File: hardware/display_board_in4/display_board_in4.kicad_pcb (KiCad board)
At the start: 4 copper layers, 250 x 50 mm, 169 parts, among them J1 CTRL, J2 HV_INPUT, J3 LED_CTRL, Q1 MMBTA42, Q10 MMBTA42, Q11 MMBTA42, Q12 MMBTA42, Q13 MMBTA42, Q14 MMBTA42, Q15 MMBTA42, Q16 MMBTA42, Q17 MMBTA42, Q18 MMBTA42, Q19 MMBTA42, Q2 MMBTA42, Q20 MMBTA42, Q21 MMBTA42, Q22 MMBTA42, Q23 MMBTA42, Q24 MMBTA42, Q25 MMBTA42, Q26 MMBTA42, Q27 MMBTA42, Q28 MMBTA42, Q29 MMBTA42, Q3 MMBTA42, Q30 MMBTA42, Q31 MMBTA42, Q32 MMBTA42, Q33 MMBTA42, Q34 MMBTA42, Q35 MMBTA42, Q36 MMBTA42, Q37 MMBTA42, Q38 MMBTA42, Q39 MMBTA42, Q4 MMBTA42, Q40 MMBTA42, Q41 MMBTA42, Q42 MMBTA42, Q43 MMBTA42, Q44 MMBTA42, Q45 MMBTA42, Q46 MMBTA42, Q47 MMBTA42, Q48 MMBTA42, Q49 MMBTA42, Q5 MMBTA42, Q50 MMBTA42, Q51 MMBTA42, Q52 MMBTA42, Q53 MMBTA42, Q54 MMBTA42, Q55 MMBTA42, Q56 MMBTA42, Q57 MMBTA42, Q58 MMBTA42, Q59 MMBTA42, Q6 MMBTA42, Q60 MMBTA42, Q7 MMBTA42, Q8 MMBTA42, Q9 MMBTA42, U1 PCA9685PW, U2 PCA9685PW, U3 PCA9685PW, U4 PCA9685PW

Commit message: WIP(hardware): update in-4 display board
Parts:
- removed GND1, GNDHV1: GND_TP, TestPoint:TestPoint_Pad_D2.0mm
- removed HV1: HV_TP, TestPoint:TestPoint_Pad_D2.0mm
- removed J3: LED_CTRL, Connector_PinSocket_2.00mm:PinSocket_2x03_P2.00mm_Vertical
- removed LG: LOGO, johnson:HR_logo_10mmx10mm
- removed REF** (x4): MountingHole_3.2mm_M3_DIN965, MountingHole:MountingHole_3.2mm_M3_DIN965
- removed SCL1: SCL_TP, TestPoint:TestPoint_Pad_D2.0mm
- removed SDA1: SDA_TP, TestPoint:TestPoint_Pad_D2.0mm
- added D25: WS2812B-2020, LED_SMD:LED_WS2812B-2020_PLCC4_2.0x2.0mm, F.Cu at (198.0, 138.5)
- added D26: WS2812B-2020, LED_SMD:LED_WS2812B-2020_PLCC4_2.0x2.0mm, F.Cu at (189.2, 142.2)
- added D27: WS2812B-2020, LED_SMD:LED_WS2812B-2020_PLCC4_2.0x2.0mm, F.Cu at (185.5, 151.0)
- added D28: WS2812B-2020, LED_SMD:LED_WS2812B-2020_PLCC4_2.0x2.0mm, F.Cu at (189.2, 159.8)
- added D29: WS2812B-2020, LED_SMD:LED_WS2812B-2020_PLCC4_2.0x2.0mm, F.Cu at (198.0, 163.5)
- added D30: WS2812B-2020, LED_SMD:LED_WS2812B-2020_PLCC4_2.0x2.0mm, F.Cu at (206.8, 159.8)
- added D31: WS2812B-2020, LED_SMD:LED_WS2812B-2020_PLCC4_2.0x2.0mm, F.Cu at (210.5, 151.0)
- added D32: WS2812B-2020, LED_SMD:LED_WS2812B-2020_PLCC4_2.0x2.0mm, F.Cu at (206.8, 142.2)
- added D33: WS2812B-2020, LED_SMD:LED_WS2812B-2020_PLCC4_2.0x2.0mm, F.Cu at (234.0, 138.5)
- added D34: WS2812B-2020, LED_SMD:LED_WS2812B-2020_PLCC4_2.0x2.0mm, F.Cu at (225.2, 142.2)
- added D35: WS2812B-2020, LED_SMD:LED_WS2812B-2020_PLCC4_2.0x2.0mm, F.Cu at (221.5, 151.0)
- added D36: WS2812B-2020, LED_SMD:LED_WS2812B-2020_PLCC4_2.0x2.0mm, F.Cu at (225.2, 159.8)
- added D37: WS2812B-2020, LED_SMD:LED_WS2812B-2020_PLCC4_2.0x2.0mm, F.Cu at (234.0, 163.5)
- added D38: WS2812B-2020, LED_SMD:LED_WS2812B-2020_PLCC4_2.0x2.0mm, F.Cu at (242.8, 159.8)
- added D39: WS2812B-2020, LED_SMD:LED_WS2812B-2020_PLCC4_2.0x2.0mm, F.Cu at (246.5, 151.0)
- added D40: WS2812B-2020, LED_SMD:LED_WS2812B-2020_PLCC4_2.0x2.0mm, F.Cu at (242.8, 142.2)
- added D41: WS2812B-2020, LED_SMD:LED_WS2812B-2020_PLCC4_2.0x2.0mm, F.Cu at (270.0, 138.5)
- added D42: WS2812B-2020, LED_SMD:LED_WS2812B-2020_PLCC4_2.0x2.0mm, F.Cu at (261.2, 142.2)
- added D43: WS2812B-2020, LED_SMD:LED_WS2812B-2020_PLCC4_2.0x2.0mm, F.Cu at (257.5, 151.0)
- added D44: WS2812B-2020, LED_SMD:LED_WS2812B-2020_PLCC4_2.0x2.0mm, F.Cu at (261.2, 159.8)
- added D45: WS2812B-2020, LED_SMD:LED_WS2812B-2020_PLCC4_2.0x2.0mm, F.Cu at (270.0, 163.5)
- added D46: WS2812B-2020, LED_SMD:LED_WS2812B-2020_PLCC4_2.0x2.0mm, F.Cu at (278.8, 159.8)
- added D47: WS2812B-2020, LED_SMD:LED_WS2812B-2020_PLCC4_2.0x2.0mm, F.Cu at (282.5, 151.0)
- added D48: WS2812B-2020, LED_SMD:LED_WS2812B-2020_PLCC4_2.0x2.0mm, F.Cu at (278.8, 142.2)
- added H1: MountingHole, MountingHole:MountingHole_3.2mm_M3_DIN965, F.Cu at (108.0, 171.0)
- added H2: MountingHole, MountingHole:MountingHole_3.2mm_M3_DIN965, F.Cu at (108.0, 131.0)
- added H3: MountingHole, MountingHole:MountingHole_3.2mm_M3_DIN965, F.Cu at (252.0, 171.0)
- added H4: MountingHole, MountingHole:MountingHole_3.2mm_M3_DIN965, F.Cu at (252.0, 131.0)
- J1: value CTRL -> Conn_02x05_Counter_Clockwise; footprint Connector_PinSocket_2.00mm:PinSocket_2x03_P2.00mm_Vertical -> Connector_PinHeader_2.00mm:PinHeader_2x05_P2.00mm_Vertical_SMD
- J2: value HV_INPUT -> Conn_02x05_Counter_Clockwise; footprint Connector_PinSocket_2.00mm:PinSocket_2x03_P2.00mm_Vertical -> Connector_PinHeader_2.00mm:PinHeader_2x05_P2.00mm_Vertical_SMD
- R1, R2: value 1.8k -> 2.2k
- R10, R11, R12, R13, R14, R15, R16, R17, R18, R19, R20, R21, R22, R23, R24, R25, R26, R27, R28, R29, R3, R30, R31, R32, R33, R34, R35, R36, R37, R38, R39, R4, R40, R41, R42, R43, R44, R45, R46, R47, R48, R49, R5, R50, R51, R52, R53, R54, R55, R56, R57, R58, R59, R6, R60, R7, R8, R9: value 1.8k -> 68k
- R61, R62: value 2.2k -> 68k
- moved J2 187.9 mm to (144.0, 167.0), turned to 0 degrees
- moved D24 150.5 mm to (170.8, 142.2), turned to -45 degrees
- moved D23 146.0 mm to (174.5, 151.0), turned to -90 degrees
- moved D21 139.5 mm to (162.0, 163.5), turned to 0 degrees
- moved D22 131.8 mm to (170.8, 159.8), turned to 45 degrees
- moved D19 131.2 mm to (149.5, 151.0), turned to 90 degrees
- moved D20 127.3 mm to (153.2, 159.8), turned to 135 degrees
- moved D18 108.4 mm to (153.2, 142.2)
- moved D16 107.0 mm to (134.8, 142.2), turned to -45 degrees
- moved D15 102.1 mm to (138.5, 151.0), turned to -90 degrees
- moved D17 102.0 mm to (162.0, 138.5), turned to 180 degrees
- moved D13 95.5 mm to (126.0, 163.5), turned to 0 degrees
- moved D14 88.4 mm to (134.8, 159.8), turned to 45 degrees
- moved D11 87.3 mm to (113.5, 151.0), turned to 90 degrees
- moved D12 83.2 mm to (117.2, 159.8), turned to 135 degrees
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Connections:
- D24 pad 1: DO -> Net-(D24-DOUT)
- J1 pad 1: +3V3 -> ANODE1
- J1 pad 2: SDA -> ANODE2
- J1 pad 3: ~{OE} -> ANODE3
- J1 pad 4: SCL -> ANODE4
- J1 pad 5: GND -> ANODE5
- J1 pad 6: GND -> ANODE6
- J2 pad 1: ANODE -> +3V3
- J2 pad 2: GND1 -> ~{OE}
- J2 pad 3: ANODE -> DI
- J2 pad 4: GND1 -> GND
- J2 pad 5: ANODE -> GND
- J2 pad 6: GND1 -> +5V
- N1 pad A3: ANODE -> ANODE1
- N2 pad A3: ANODE -> ANODE2
- N3 pad A3: ANODE -> ANODE3
- N4 pad A3: ANODE -> ANODE4
- N5 pad A3: ANODE -> ANODE5
- N6 pad A3: ANODE -> ANODE6
- R1 pad 1: GND1 -> +3V3
- R1 pad 2: /N1_E0 -> SDA
- R10 pad 1: GND1 -> GND
- R10 pad 2: /N1_E9 -> /N1_E7
- R11 pad 1: GND1 -> GND
- R11 pad 2: /N2_E0 -> /N1_E8
- R12 pad 1: GND1 -> GND
- R12 pad 2: /N2_E1 -> /N1_E9
- R13 pad 1: GND1 -> GND
- R13 pad 2: /N2_E2 -> /N2_E0
- R14 pad 1: GND1 -> GND
- R14 pad 2: /N2_E3 -> /N2_E1
- R15 pad 1: GND1 -> GND
- R15 pad 2: /N2_E4 -> /N2_E2
- R16 pad 1: GND1 -> GND
- R16 pad 2: /N2_E5 -> /N2_E3
- R17 pad 1: GND1 -> GND
- R17 pad 2: /N2_E6 -> /N2_E4
- R18 pad 1: GND1 -> GND
- R18 pad 2: /N2_E7 -> /N2_E5
- R19 pad 1: GND1 -> GND
- R19 pad 2: /N2_E8 -> /N2_E6
- R2 pad 1: GND1 -> +3V3
- R2 pad 2: /N1_E1 -> SCL
- R20 pad 1: GND1 -> GND
- R20 pad 2: /N2_E9 -> /N2_E7
- R21 pad 1: GND1 -> GND
- R21 pad 2: /N3_E0 -> /N2_E8
- R22 pad 1: GND1 -> GND
- R22 pad 2: /N3_E1 -> /N2_E9
- R23 pad 1: GND1 -> GND
- R23 pad 2: /N3_E2 -> /N3_E0
- R24 pad 1: GND1 -> GND
- R24 pad 2: /N3_E3 -> /N3_E1
- R25 pad 1: GND1 -> GND
- R25 pad 2: /N3_E4 -> /N3_E2
- R26 pad 1: GND1 -> GND
- R26 pad 2: /N3_E5 -> /N3_E3
- R27 pad 1: GND1 -> GND
- R27 pad 2: /N3_E6 -> /N3_E4
- R28 pad 1: GND1 -> GND
- R28 pad 2: /N3_E7 -> /N3_E5
- R29 pad 1: GND1 -> GND
- R29 pad 2: /N3_E8 -> /N3_E6
- R3 pad 1: GND1 -> GND
- R3 pad 2: /N1_E2 -> /N1_E0
- R30 pad 1: GND1 -> GND
- R30 pad 2: /N3_E9 -> /N3_E7
- R31 pad 1: GND1 -> GND
- R31 pad 2: /N4_E0 -> /N3_E8
- R32 pad 1: GND1 -> GND
- R32 pad 2: /N4_E1 -> /N3_E9
- R33 pad 1: GND1 -> GND
- R33 pad 2: /N4_E2 -> /N4_E0
- R34 pad 1: GND1 -> GND
- R34 pad 2: /N4_E3 -> /N4_E1
- R35 pad 1: GND1 -> GND
- R35 pad 2: /N4_E4 -> /N4_E2
- R36 pad 1: GND1 -> GND
- R36 pad 2: /N4_E5 -> /N4_E3
- R37 pad 1: GND1 -> GND
- R37 pad 2: /N4_E6 -> /N4_E4
- R38 pad 1: GND1 -> GND
- R38 pad 2: /N4_E7 -> /N4_E5
- R39 pad 1: GND1 -> GND
- R39 pad 2: /N4_E8 -> /N4_E6
- R4 pad 1: GND1 -> GND
- R4 pad 2: /N1_E3 -> /N1_E1
- R40 pad 1: GND1 -> GND
- R40 pad 2: /N4_E9 -> /N4_E7
- R41 pad 1: GND1 -> GND
- R41 pad 2: /N5_E0 -> /N4_E8
- R42 pad 1: GND1 -> GND
- R42 pad 2: /N5_E1 -> /N4_E9
- R43 pad 1: GND1 -> GND
- R43 pad 2: /N5_E2 -> /N5_E0
- R44 pad 1: GND1 -> GND
- R44 pad 2: /N5_E3 -> /N5_E1
- R45 pad 1: GND1 -> GND
- R45 pad 2: /N5_E4 -> /N5_E2
- R46 pad 1: GND1 -> GND
- R46 pad 2: /N5_E5 -> /N5_E3
- R47 pad 1: GND1 -> GND
- R47 pad 2: /N5_E6 -> /N5_E4
- R48 pad 1: GND1 -> GND
- R48 pad 2: /N5_E7 -> /N5_E5
- R49 pad 1: GND1 -> GND
- R49 pad 2: /N5_E8 -> /N5_E6
- R5 pad 1: GND1 -> GND
- R5 pad 2: /N1_E4 -> /N1_E2
- R50 pad 1: GND1 -> GND
- R50 pad 2: /N5_E9 -> /N5_E7
- R51 pad 1: GND1 -> GND
- R51 pad 2: /N6_E0 -> /N5_E8
- R52 pad 1: GND1 -> GND
- R52 pad 2: /N6_E1 -> /N5_E9
- R53 pad 1: GND1 -> GND
- R53 pad 2: /N6_E2 -> /N6_E0
- R54 pad 1: GND1 -> GND
- R54 pad 2: /N6_E3 -> /N6_E1
- R55 pad 1: GND1 -> GND
- R55 pad 2: /N6_E4 -> /N6_E2
- R56 pad 1: GND1 -> GND
- R56 pad 2: /N6_E5 -> /N6_E3
- R57 pad 1: GND1 -> GND
- R57 pad 2: /N6_E6 -> /N6_E4
- R58 pad 1: GND1 -> GND
- R58 pad 2: /N6_E7 -> /N6_E5
- R59 pad 1: GND1 -> GND
- R59 pad 2: /N6_E8 -> /N6_E6
- R6 pad 1: GND1 -> GND
- R6 pad 2: /N1_E5 -> /N1_E3
- R60 pad 1: GND1 -> GND
- R60 pad 2: /N6_E9 -> /N6_E7
- R61 pad 1: +3V3 -> GND
- R61 pad 2: SDA -> /N6_E8
- R62 pad 1: +3V3 -> GND
- R62 pad 2: SCL -> /N6_E9
- R7 pad 1: GND1 -> GND
- R7 pad 2: /N1_E6 -> /N1_E4
- R8 pad 1: GND1 -> GND
- R8 pad 2: /N1_E7 -> /N1_E5
- R9 pad 1: GND1 -> GND
- R9 pad 2: /N1_E8 -> /N1_E6
- U2 pad 21: unconnected-(U2-LED14-Pad21) -> /N4_B0
- U2 pad 22: unconnected-(U2-LED15-Pad22) -> /N4_B1
- U3 pad 10: /N4_B4 -> /N4_B6
- U3 pad 11: /N4_B5 -> /N4_B7
- U3 pad 12: /N4_B6 -> /N4_B8
- U3 pad 13: /N4_B7 -> /N4_B9
- U3 pad 15: /N4_B8 -> /N5_B0
- U3 pad 16: /N4_B9 -> /N5_B1
- U3 pad 17: /N5_B0 -> /N5_B2
- U3 pad 18: /N5_B1 -> /N5_B3
- U3 pad 19: /N5_B2 -> /N5_B4
- U3 pad 20: /N5_B3 -> /N5_B5
- U3 pad 21: /N5_B4 -> /N5_B6
- U3 pad 22: /N5_B5 -> /N5_B7
- U3 pad 6: /N4_B0 -> /N4_B2
- U3 pad 7: /N4_B1 -> /N4_B3
- U3 pad 8: /N4_B2 -> /N4_B4
- U3 pad 9: /N4_B3 -> /N4_B5
- U4 pad 10: /N6_B0 -> /N6_B2
- U4 pad 11: /N6_B1 -> /N6_B3
- U4 pad 12: /N6_B2 -> /N6_B4
- U4 pad 13: /N6_B3 -> /N6_B5
- U4 pad 15: /N6_B4 -> /N6_B6
- U4 pad 16: /N6_B5 -> /N6_B7
- U4 pad 17: /N6_B6 -> /N6_B8
- U4 pad 18: /N6_B7 -> /N6_B9
- U4 pad 19: /N6_B8 -> unconnected-(U4-LED12-Pad19)
- U4 pad 20: /N6_B9 -> unconnected-(U4-LED13-Pad20)
- U4 pad 6: /N5_B6 -> /N5_B8
- U4 pad 7: /N5_B7 -> /N5_B9
- U4 pad 8: /N5_B8 -> /N6_B0
- U4 pad 9: /N5_B9 -> /N6_B1
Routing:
- net ANODE: track 385.7 -> 0.00 mm
- net DO: track 250.9 -> 0.00 mm, vias 1 -> 0
- net SDA: track 191.1 -> 0.00 mm, vias 5 -> 0
- net SCL: track 186.0 -> 0.00 mm, vias 5 -> 0
- net GND1: track 166.2 -> 0.00 mm, vias 47 -> 0
- net +5V: track 530.1 -> 685.6 mm, vias 3 -> 1
- net DI: track 14.1 -> 110.4 mm, vias 0 -> 1
- net /N1_B5: track 42.4 -> 120.6 mm, vias 2 -> 0
- net /N6_B6: track 76.0 -> 0.00 mm
- net GND: track 74.6 -> 0.00 mm, vias 36 -> 0
- net /N3_B4: track 73.1 -> 0.00 mm
- net /N4_B3: track 70.8 -> 0.00 mm
- net /N6_B4: track 65.8 -> 0.00 mm, vias 2 -> 0
- net /N3_B6: track 63.9 -> 0.00 mm
- net /N6_B8: track 59.7 -> 0.00 mm, vias 2 -> 0
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- removed copper zone on In2.Cu, net GND
- removed copper zone on In1.Cu, net GND1
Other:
- board size 250 x 50 mm -> 230 x 50 mm

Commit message: WIP(hardware): in4 display board layout
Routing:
- net SCL: track 0.00 -> 164.0 mm, vias 0 -> 7
- net SDA: track 0.00 -> 153.1 mm, vias 0 -> 7
- net ANODE1: track 0.00 -> 131.7 mm, vias 0 -> 2
- net ANODE2: track 0.00 -> 98.8 mm, vias 0 -> 3
- net /N6_B9: track 0.00 -> 89.5 mm, vias 0 -> 3
- net /N6_B7: track 0.00 -> 86.9 mm, vias 0 -> 2
- net ANODE6: track 0.00 -> 84.8 mm, vias 0 -> 3
- net /N6_B2: track 0.00 -> 77.1 mm, vias 0 -> 4
- net /N6_B8: track 0.00 -> 74.0 mm, vias 0 -> 2
- net /N5_B0: track 0.00 -> 73.2 mm
- net /N2_B7: track 0.00 -> 71.4 mm, vias 0 -> 2
- net /N6_B0: track 0.00 -> 70.9 mm, vias 0 -> 2
- net /N5_B6: track 0.00 -> 69.9 mm
- net /N6_B1: track 0.00 -> 68.5 mm, vias 0 -> 2
- net /N5_B2: track 0.00 -> 68.1 mm, vias 0 -> 2
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
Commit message: WIP(hardware): in4 display board layout
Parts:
- removed J2: Conn_02x05_Counter_Clockwise, Connector_PinHeader_2.00mm:PinHeader_2x05_P2.00mm_Vertical_SMD
- added J3: Conn_02x05_Odd_Even, Connector_PinSocket_2.00mm:PinSocket_2x05_P2.00mm_Vertical_SMD, B.Cu at (216.0, 136.0)
- J1: value Conn_02x05_Counter_Clockwise -> Conn_02x05_Odd_Even; footprint Connector_PinHeader_2.00mm:PinHeader_2x05_P2.00mm_Vertical_SMD -> Connector_PinSocket_2.00mm:PinSocket_2x05_P2.00mm_Vertical_SMD
- moved J1 77.9 mm to (145.0, 167.0), turned to 0 degrees
- moved R1 0.25 mm to (151.0, 170.2)
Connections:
- J1 pad 1: ANODE1 -> SDA
- J1 pad 2: ANODE2 -> +3V3
- J1 pad 3: ANODE3 -> SCL
- J1 pad 4: ANODE4 -> ~{OE}
- J1 pad 5: ANODE5 -> GND
- J1 pad 6: ANODE6 -> DI
- J1 pad 7: unconnected-(J1-Pin_7-Pad7) -> GND
- J1 pad 9: GND -> +5V
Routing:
- net GND: track 0.00 -> 566.1 mm, vias 0 -> 86
- net /N5_B7: track 0.00 -> 76.3 mm, vias 0 -> 2
- net /N2_B3: track 0.00 -> 47.8 mm, vias 0 -> 2
- net SDA: track 153.1 -> 165.1 mm, vias 7 -> 6
- net ANODE6: track 84.8 -> 73.6 mm
- net DI: track 110.4 -> 101.1 mm
- net +5V: track 695.8 -> 703.8 mm
- net /N1_B5: track 120.6 -> 112.8 mm
- net ~{OE}: track 170.8 -> 176.7 mm
- net ANODE5: track 57.7 -> 52.5 mm
- net ANODE3: track 64.1 -> 68.9 mm, vias 3 -> 1
- net /N6_B8: track 74.0 -> 69.9 mm
- net ANODE2: track 98.8 -> 102.1 mm
- net /N6_B9: track 89.5 -> 86.5 mm
- net ANODE4: track 19.5 -> 22.3 mm, vias 0 -> 1
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- added copper zone on In2.Cu, net GND

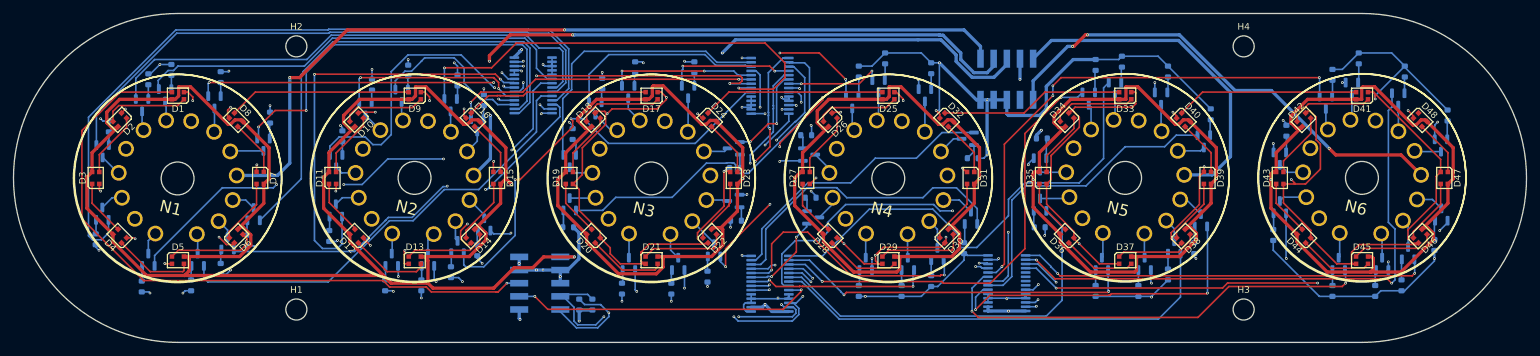
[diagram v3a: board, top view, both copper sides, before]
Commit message: hardware(schematic): Update IN-4 schematic and layout
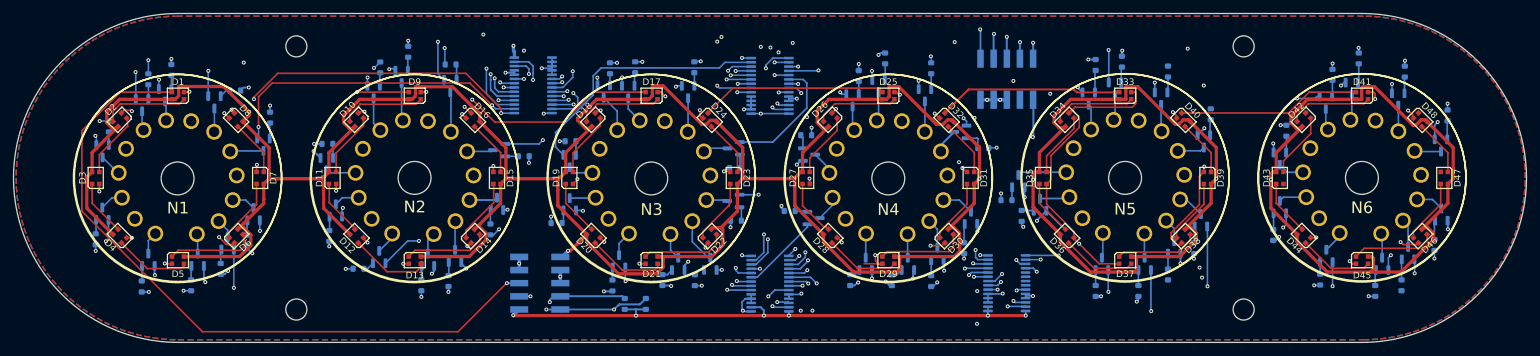
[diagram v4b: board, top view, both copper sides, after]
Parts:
- added G***: LOGO, habonroof_kicad_library:HR_logo_6mmx6mm, B.Cu at (131.2, 171.5)
- moved R46 10.8 mm to (215.9, 154.4)
- moved R22 10.5 mm to (142.6, 147.7), turned to 180 degrees
- moved R1 10.1 mm to (161.1, 170.2)
- moved Q20 5.03 mm to (138.8, 146.8), turned to 180 degrees
- moved R2 4.93 mm to (157.9, 170.2)
- moved R14 4.77 mm to (117.5, 164.8), turned to 0 degrees
- moved Q44 4.17 mm to (217.8, 151.5), turned to 90 degrees
- moved R38 3.77 mm to (183.0, 156.0), turned to 0 degrees
- moved R21 3.75 mm to (137.5, 158.8)
- moved Q19 3.68 mm to (138.5, 154.9)
- moved R48 3.25 mm to (218.2, 156.8), turned to 90 degrees
- moved R10 2.99 mm to (98.7, 137.7), turned to 180 degrees
- moved Q18 2.91 mm to (131.4, 137.0)
- moved Q13 2.91 mm to (119.8, 137.9)
- moved R15 2.91 mm to (120.8, 134.2)
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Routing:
- net GND: track 566.1 -> 216.4 mm, vias 86 -> 111
- net +5V: track 703.8 -> 623.5 mm, vias 9 -> 5
- net /N2_B5: track 65.4 -> 40.9 mm
- net /N5_B1: track 54.3 -> 77.5 mm, vias 2 -> 3
- net /N2_B8: track 67.1 -> 45.6 mm, vias 3 -> 2
- net /N1_B5: track 112.8 -> 95.5 mm, vias 0 -> 2
- net /N1_B6: track 61.3 -> 76.6 mm
- net /N1_B7: track 55.9 -> 70.1 mm, vias 3 -> 2
- net /N1_B9: track 61.8 -> 47.8 mm
- net /N5_B0: track 73.1 -> 86.4 mm, vias 0 -> 3
- net /N4_B7: track 49.5 -> 62.4 mm, vias 4 -> 3
- net /N4_B2: track 54.3 -> 41.8 mm, vias 3 -> 2
- net /N6_B0: track 70.9 -> 82.9 mm, vias 2 -> 4
- net /N6_B3: track 59.2 -> 71.1 mm, vias 2 -> 3
- net /N5_B5: track 59.6 -> 48.0 mm, vias 0 -> 2
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- added copper zone on B.Cu, net GND
- added copper zone on F.Cu, net GND
- added copper zone on In1.Cu, net GND
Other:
- board text added: "5V GND GND SCL SDA"
- board text added: "A1 A2 A3 A4 A5"
- board text added: "GND GND DI ~{OE} 3V3"
- board text added: "GND GND GND X A6"
- board text added: "IN-4 Display Board V0.9.0"

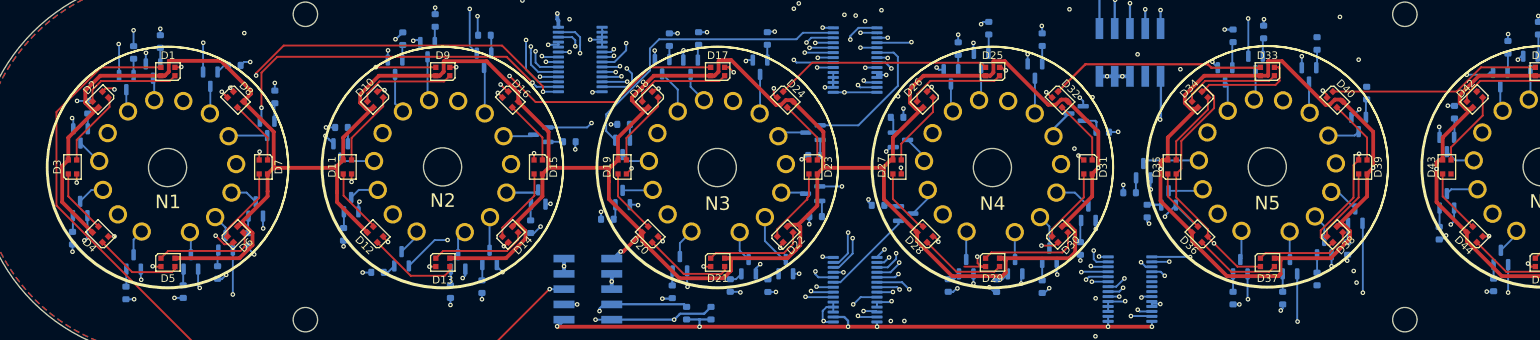
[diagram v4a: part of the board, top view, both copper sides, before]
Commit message: hardware(display): fix the rotation of IN-4 tube
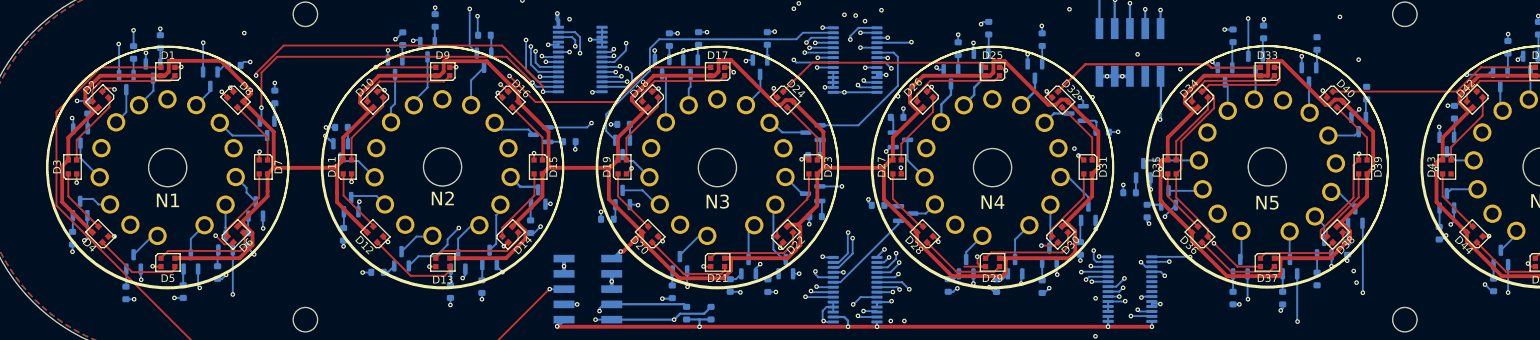
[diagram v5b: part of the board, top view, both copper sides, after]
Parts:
- turned N1 to 0 degrees
- turned N2 to 0 degrees
- turned N3 to 0 degrees
- turned N4 to 0 degrees
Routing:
- net /N5_B5: track 48.0 -> 44.7 mm
- net /N2_D4: track 3.32 -> 5.62 mm
- net /N2_D6: track 4.37 -> 6.56 mm
- net /N4_D3: track 3.67 -> 5.82 mm
- net /N1_D3: track 3.42 -> 5.52 mm
- net ANODE4: track 33.2 -> 31.2 mm
- net ANODE2: track 104.8 -> 102.8 mm
- net ANODE1: track 136.2 -> 134.3 mm
- net ANODE3: track 70.4 -> 68.5 mm
- net /N1_D2: track 2.95 -> 4.83 mm
- net /N1_D9: track 5.09 -> 6.90 mm
- net /N4_D4: track 3.60 -> 5.33 mm
- net /N3_D5: track 3.96 -> 5.64 mm
- net /N1_D4: track 3.01 -> 4.61 mm
- net /N4_D0: track 4.37 -> 5.85 mm
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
